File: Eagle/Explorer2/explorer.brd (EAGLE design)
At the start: 101.6 x 66 mm, 10 parts

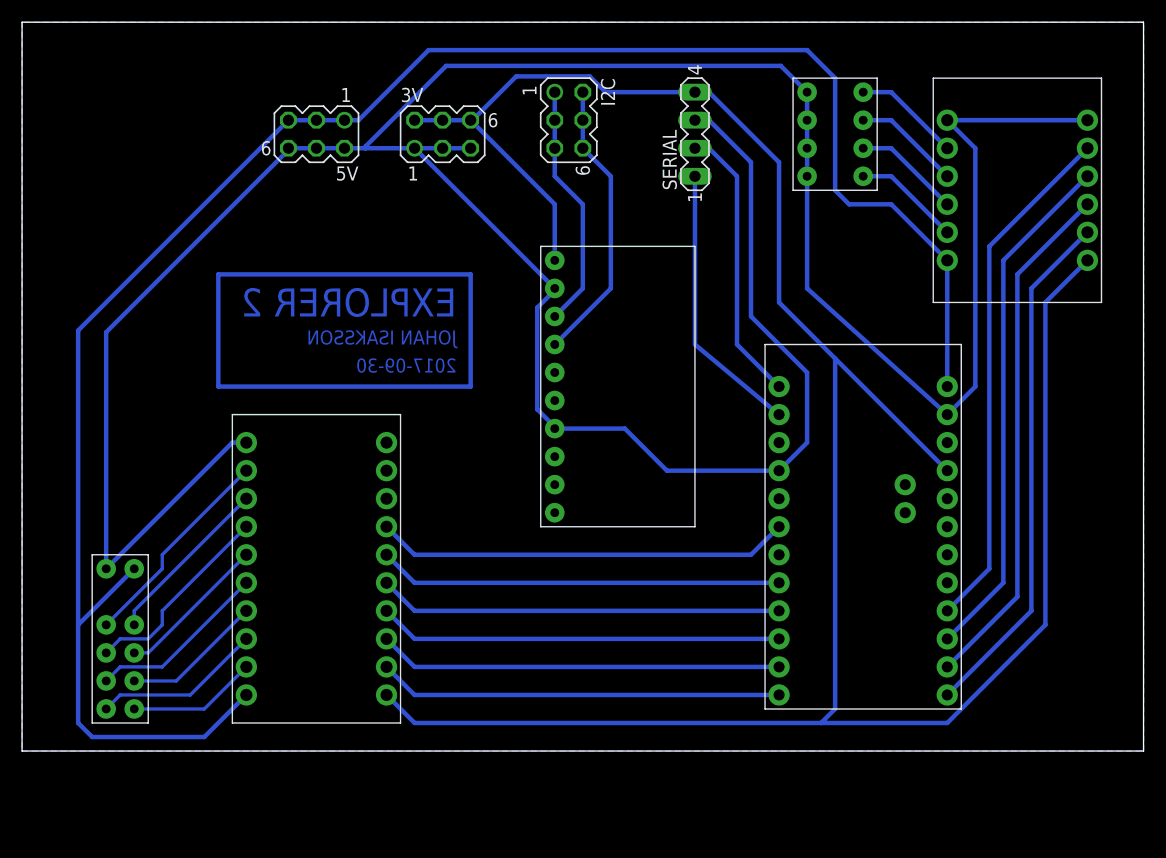
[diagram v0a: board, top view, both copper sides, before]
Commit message: Redesigned Explorer2 board to use two copper layers. Cleaned up and tested Explorer2 code, ready for test.
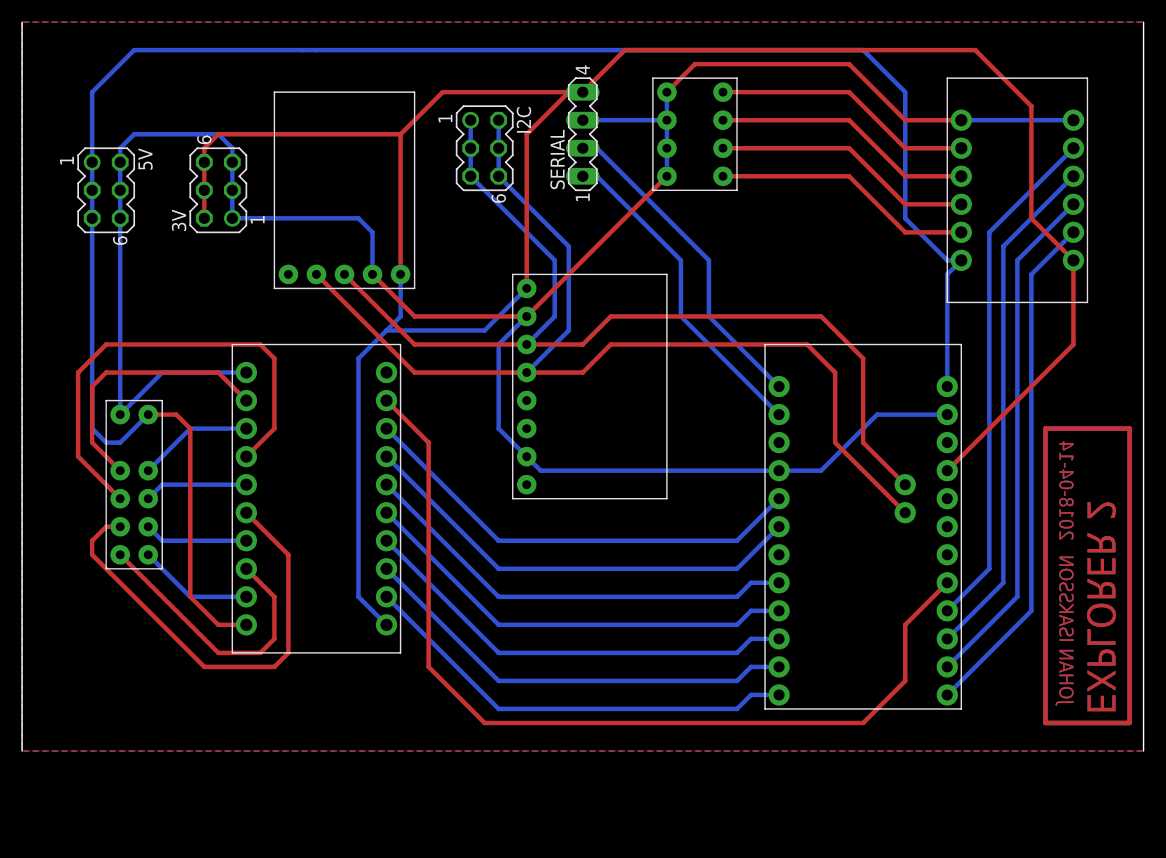
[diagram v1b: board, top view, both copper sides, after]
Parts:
- added U$5: LEVELSHIFT_4CH, quadcopter_comp:LEVELSHIFT_4CH
- U$2: value MPU9250 -> MPU6050; device quadcopter_comp:MPU9250 -> quadcopter_comp:MPU6050
- U$7: value LEVELSHIFT_4CH -> HMC5883L; device quadcopter_comp:LEVELSHIFT_4CH -> quadcopter_comp:HMC5883L
- moved U$7 61.0 mm to (29.2, 50.8), turned to 270 degrees
- moved 3V 20.9 mm to (17.8, 50.8), turned to 90 degrees
- moved 5V 19.7 mm to (7.62, 50.8), turned to 270 degrees
- moved U$6 14.0 mm to (10.2, 24.1)
- moved U$1 12.7 mm to (61.0, 55.9)
- moved SERIAL 10.2 mm to (50.8, 55.9)
- moved I2C 8.03 mm to (41.9, 54.6)
- moved U$4 6.35 mm to (26.7, 22.9)
- moved U$2 2.54 mm to (52.1, 33.0)
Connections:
- new net N$19: U$3.2, U$4.A7
- new net N$25: U$3.A0, U$4.A8
- net 3V: now also U$5.LV, U$7.VCC; no longer U$7.LV
- net 5V: now also U$5.HV; no longer U$7.HV
- net GND: now also U$5.GND, U$5.GND2; no longer U$7.GND2
- net N$1: now also U$5.B4; no longer U$7.B4
- net N$10: now also U$5.A4; no longer U$7.A4
- net N$2: now also U$5.B3; no longer U$7.B3
- net N$26: now also U$7.SCL
- net N$28: now also U$7.SDA
- net N$3: now also U$5.B2; no longer U$7.B2
- net N$4: now also U$5.B1; no longer U$7.B1
- net N$7: now also U$5.A1; no longer U$7.A1
- net N$8: now also U$5.A2; no longer U$7.A2
- net N$9: now also U$5.A3; no longer U$7.A3
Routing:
- net N$25: track 0.00 -> 83.0 mm
- net GND: track 291.0 -> 216.0 mm
- net N$28: track 26.0 -> 95.2 mm
- net N$29: track 0.00 -> 68.6 mm
- net N$27: track 0.00 -> 68.6 mm
- net N$26: track 22.6 -> 89.8 mm
- net N$5: track 66.0 -> 0.00 mm
- net N$19: track 0.00 -> 41.3 mm
- net N$14: track 16.4 -> 41.1 mm
- net N$16: track 18.2 -> 42.3 mm
- net N$4: track 9.72 -> 23.7 mm
- net N$3: track 9.72 -> 23.7 mm
- net N$2: track 9.72 -> 23.7 mm
- net N$1: track 9.72 -> 23.7 mm
- net 3V: track 220.7 -> 207.1 mm
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- added copper zone on layer 1, net GND
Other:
- board text added: "2018-04-14"
- board text removed: "2017-09-30"

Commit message: Replaced all sensor breakout boards with one gy-86 board. Started on pids for altitude hold.
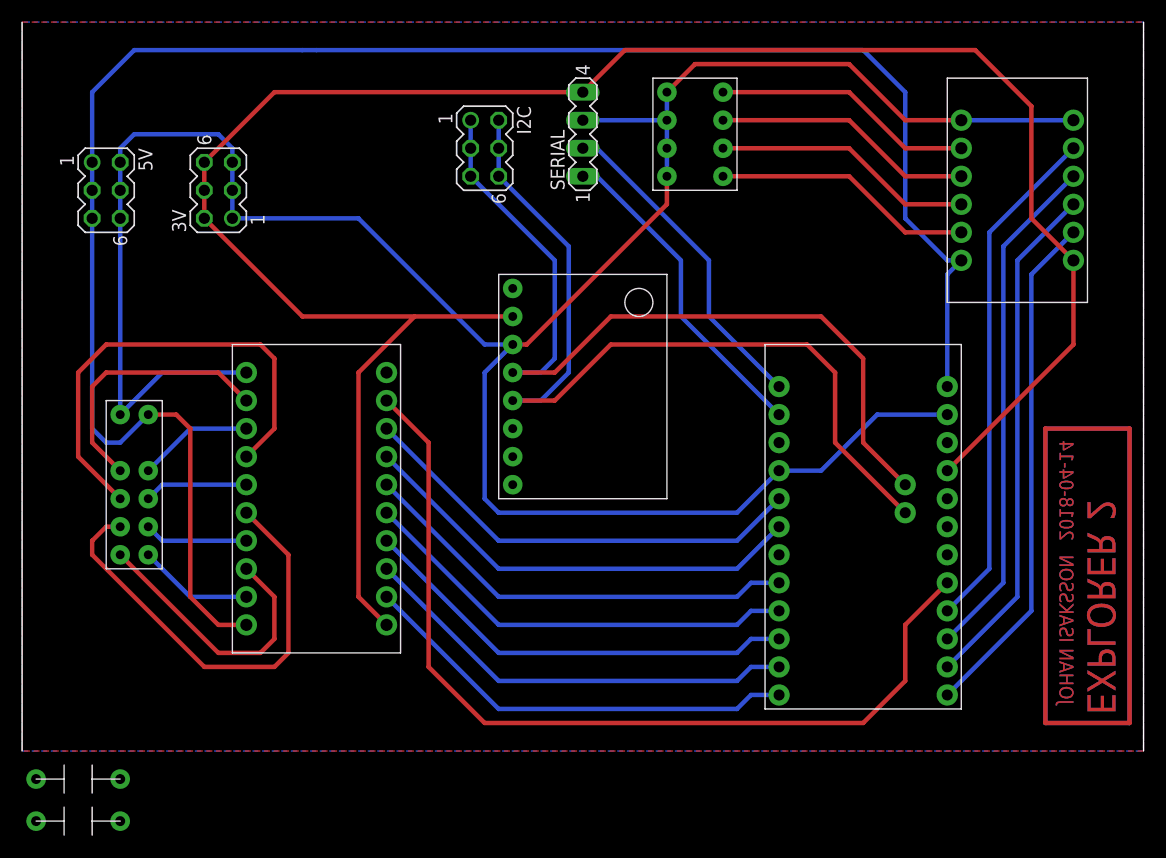
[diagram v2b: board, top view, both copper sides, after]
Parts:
- added U$8: GY-86, quadcopter_comp:GY-86
- U$2: value MPU6050 -> CAP; device quadcopter_comp:MPU6050 -> quadcopter_comp:CAP
- U$7: value HMC5883L -> CAP; device quadcopter_comp:HMC5883L -> quadcopter_comp:CAP
- moved U$7 62.0 mm to (5.08, -6.35), turned to 0 degrees
- moved U$2 58.9 mm to (5.08, -2.54)
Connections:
- net 3V: now also U$8.3V3; no longer U$2.VCC, U$7.VCC
- net 5V: now also U$2.B, U$7.B
- net GND: now also U$2.A, U$7.A, U$8.GND; no longer U$2.AD0, U$2.GND, U$7.GND
- net N$26: now also U$8.SCL; no longer U$2.SCL, U$7.SCL
- net N$28: now also U$8.SDA; no longer U$2.SDA, U$7.SDA
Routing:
- net 3V: track 207.1 -> 188.4 mm
- net N$28: track 95.2 -> 79.3 mm
- net N$26: track 89.8 -> 77.5 mm
- net GND: track 216.0 -> 223.0 mm
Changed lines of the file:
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@@
 <attribute name="MF" value="" x="50.8" y="55.88" size="1.778" layer="27" rot="R90" display="off"/>
 </element>
-<element name="U$2" library="quadcopter_comp" package="MPU6050" value="MPU6050" x="52.07" y="33.02"/>
 <element name="U$5" library="quadcopter_comp" package="LEVELSHIFT_4CH" value="LEVELSHIFT_4CH" x="90.17" y="50.8" rot="R180"/>
-<element name="U$7" library="quadcopter_comp" package="HMC5883L" value="HMC5883L" x="29.21" y="50.8" rot="R270"/>
+<element name="U$8" library="quadcopter_comp" package="GY-86" value="GY-86" x="50.8" y="33.02"/>
+<element name="U$2" library="quadcopter_comp" package="CAP" value="CAP" x="5.08" y="-2.54"/>
+<element name="U$7" library="quadcopter_comp" package="CAP" value="CAP" x="5.08" y="-6.35"/>
 </elements>
 <signals>
@@
 <vertex x="0" y="0"/>
 </polygon>
-<contactref element="U$2" pad="GND"/>
-<contactref element="U$2" pad="AD0"/>
 <contactref element="U$5" pad="GND2"/>
 <contactref element="U$5" pad="GND"/>
@@
 <wire x1="74.93" y1="62.23" x2="60.96" y2="62.23" width="0.4064" layer="1"/>
 <wire x1="60.96" y1="62.23" x2="58.42" y2="59.69" width="0.4064" layer="1"/>
-<wire x1="68.58" y1="25.4" x2="46.99" y2="25.4" width="0.4064" layer="16"/>
-<wire x1="46.99" y1="25.4" x2="45.72" y2="26.67" width="0.4064" layer="16"/>
-<wire x1="45.72" y1="39.37" x2="43.18" y2="36.83" width="0.4064" layer="16"/>
-<wire x1="43.18" y1="36.83" x2="43.18" y2="29.21" width="0.4064" layer="16"/>
-<wire x1="43.18" y1="29.21" x2="45.72" y2="26.67" width="0.4064" layer="16"/>
-<wire x1="45.72" y1="39.37" x2="58.42" y2="52.07" width="0.4064" layer="1"/>
-<contactref element="U$7" pad="GND"/>
 <wire x1="8.89" y1="30.48" x2="8.89" y2="48.26" width="0.4064" layer="16"/>
 <wire x1="8.89" y1="50.8" x2="8.89" y2="48.26" width="0.4064" layer="16"/>
 <wire x1="8.89" y1="53.34" x2="8.89" y2="50.8" width="0.4064" layer="16"/>
-<wire x1="31.75" y1="43.18" x2="31.75" y2="46.99" width="0.4064" layer="16"/>
-<wire x1="31.75" y1="46.99" x2="30.48" y2="48.26" width="0.4064" layer="16"/>
 <wire x1="30.48" y1="48.26" x2="19.05" y2="48.26" width="0.4064" layer="16"/>
 <wire x1="19.05" y1="50.8" x2="19.05" y2="48.26" width="0.4064" layer="16"/>
@@
 <wire x1="17.78" y1="55.88" x2="19.05" y2="54.61" width="0.4064" layer="16"/>
 <wire x1="19.05" y1="54.61" x2="19.05" y2="53.34" width="0.4064" layer="16"/>
-<wire x1="31.75" y1="43.18" x2="35.56" y2="39.37" width="0.4064" layer="1"/>
-<wire x1="35.56" y1="39.37" x2="45.72" y2="39.37" width="0.4064" layer="1"/>
+<contactref element="U$8" pad="GND"/>
+<wire x1="30.48" y1="48.26" x2="41.91" y2="36.83" width="0.4064" layer="16"/>
+<wire x1="41.91" y1="36.83" x2="44.45" y2="36.83" width="0.4064" layer="16"/>
+<wire x1="44.45" y1="36.83" x2="45.72" y2="36.83" width="0.4064" layer="1"/>
+<wire x1="45.72" y1="36.83" x2="58.42" y2="49.53" width="0.4064" layer="1"/>
+<wire x1="58.42" y1="49.53" x2="58.42" y2="52.07" width="0.4064" layer="1"/>
+<wire x1="44.45" y1="36.83" x2="41.91" y2="34.29" width="0.4064" layer="16"/>
+<wire x1="41.91" y1="34.29" x2="41.91" y2="22.86" width="0.4064" layer="16"/>
+<wire x1="41.91" y1="22.86" x2="43.18" y2="21.59" width="0.4064" layer="16"/>
+<wire x1="43.18" y1="21.59" x2="64.77" y2="21.59" width="0.4064" layer="16"/>
+<wire x1="64.77" y1="21.59" x2="68.58" y2="25.4" width="0.4064" layer="16"/>
+<contactref element="U$2" pad="A"/>
+<contactref element="U$7" pad="A"/>
+<wire x1="1.27" y1="-2.54" x2="8.89" y2="30.48" width="0" layer="19" extent="1-1"/>
+<wire x1="1.27" y1="-6.35" x2="1.27" y2="-2.54" width="0" layer="19" extent="1-1"/>
 </signal>
 <signal name="N$20">
@@
 <wire x1="6.35" y1="59.69" x2="10.16" y2="63.5" width="0.4064" layer="16"/>
 <wire x1="10.16" y1="63.5" x2="25.4" y2="63.5" width="0.4064" layer="16"/>
+<contactref element="U$2" pad="B"/>
+<contactref element="U$7" pad="B"/>
+<wire x1="8.89" y1="-2.54" x2="17.78" y2="11.43" width="0" layer="19" extent="1-1"/>
+<wire x1="8.89" y1="-6.35" x2="8.89" y2="-2.54" width="0" layer="19" extent="1-1"/>
 </signal>
 <signal name="3V">
@@
 <contactref element="3V" pad="4"/>
 <contactref element="SERIAL" pad="4"/>
-<wire x1="33.02" y1="11.43" x2="30.48" y2="13.97" width="0.4064" layer="16"/>
-<wire x1="30.48" y1="13.97" x2="30.48" y2="35.56" width="0.4064" layer="16"/>
-<wire x1="30.48" y1="35.56" x2="33.02" y2="38.1" width="0.4064" layer="16"/>
-<wire x1="33.02" y1="38.1" x2="41.91" y2="38.1" width="0.4064" layer="16"/>
-<wire x1="34.29" y1="55.88" x2="38.1" y2="59.69" width="0.4064" layer="1"/>
-<wire x1="38.1" y1="59.69" x2="49.53" y2="59.69" width="0.4064" layer="1"/>
-<wire x1="49.53" y1="59.69" x2="50.8" y2="59.69" width="0.4064" layer="1"/>
 <wire x1="54.61" y1="63.5" x2="50.8" y2="59.69" width="0.4064" layer="1"/>
-<contactref element="U$2" pad="VCC"/>
 <contactref element="U$5" pad="LV"/>
 <wire x1="54.61" y1="63.5" x2="86.36" y2="63.5" width="0.4064" layer="1"/>
@@
 <wire x1="95.25" y1="44.45" x2="95.25" y2="36.83" width="0.4064" layer="1"/>
 <wire x1="95.25" y1="36.83" x2="83.82" y2="25.4" width="0.4064" layer="1"/>
-<wire x1="41.91" y1="38.1" x2="45.72" y2="41.91" width="0.4064" layer="16"/>
-<wire x1="45.72" y1="41.91" x2="45.72" y2="55.88" width="0.4064" layer="1"/>
-<wire x1="45.72" y1="55.88" x2="49.53" y2="59.69" width="0.4064" layer="1"/>
-<contactref element="U$7" pad="VCC"/>
-<wire x1="34.29" y1="43.18" x2="34.29" y2="39.37" width="0.4064" layer="16"/>
-<wire x1="34.29" y1="39.37" x2="33.02" y2="38.1" width="0.4064" layer="16"/>
 <wire x1="16.51" y1="53.34" x2="16.51" y2="50.8" width="0.4064" layer="1"/>
-<wire x1="34.29" y1="43.18" x2="34.29" y2="55.88" width="0.4064" layer="1"/>
-<wire x1="16.51" y1="53.34" x2="16.51" y2="54.61" width="0.4064" layer="1"/>
-<wire x1="16.51" y1="54.61" x2="17.78" y2="55.88" width="0.4064" layer="1"/>
-<wire x1="17.78" y1="55.88" x2="34.29" y2="55.88" width="0.4064" layer="1"/>
 <wire x1="16.51" y1="50.8" x2="16.51" y2="48.26" width="0.4064" layer="1"/>
+<contactref element="U$8" pad="3V3"/>
+<wire x1="22.86" y1="59.69" x2="16.51" y2="53.34" width="0.4064" layer="1"/>
+<wire x1="50.8" y1="59.69" x2="22.86" y2="59.69" width="0.4064" layer="1"/>
+<wire x1="44.45" y1="39.37" x2="35.56" y2="39.37" width="0.4064" layer="1"/>
+<wire x1="35.56" y1="39.37" x2="25.4" y2="39.37" width="0.4064" layer="1"/>
+<wire x1="25.4" y1="39.37" x2="16.51" y2="48.26" width="0.4064" layer="1"/>
+<wire x1="33.02" y1="11.43" x2="30.48" y2="13.97" width="0.4064" layer="1"/>
+<wire x1="30.48" y1="13.97" x2="30.48" y2="34.29" width="0.4064" layer="1"/>
+<wire x1="30.48" y1="34.29" x2="35.56" y2="39.37" width="0.4064" layer="1"/>
 </signal>
 <signal name="N$26">
@@
 <wire x1="76.2" y1="27.94" x2="76.2" y2="35.56" width="0.4064" layer="1"/>
 <wire x1="76.2" y1="35.56" x2="72.39" y2="39.37" width="0.4064" layer="1"/>
-<contactref element="U$2" pad="SCL"/>
 <wire x1="72.39" y1="39.37" x2="53.34" y2="39.37" width="0.4064" layer="1"/>
-<wire x1="53.34" y1="39.37" x2="50.8" y2="36.83" width="0.4064" layer="1"/>
-<wire x1="50.8" y1="36.83" x2="45.72" y2="36.83" width="0.4064" layer="1"/>
 <wire x1="40.64" y1="52.07" x2="48.26" y2="44.45" width="0.4064" layer="16"/>
-<wire x1="48.26" y1="44.45" x2="48.26" y2="39.37" width="0.4064" layer="16"/>
-<wire x1="48.26" y1="39.37" x2="45.72" y2="36.83" width="0.4064" layer="16"/>
-<contactref element="U$7" pad="SCL"/>
-<wire x1="45.72" y1="36.83" x2="35.56" y2="36.83" width="0.4064" layer="1"/>
-<wire x1="35.56" y1="36.83" x2="29.21" y2="43.18" width="0.4064" layer="1"/>
+<wire x1="48.26" y1="44.45" x2="48.26" y2="35.56" width="0.4064" layer="16"/>
+<contactref element="U$8" pad="SCL"/>
+<wire x1="53.34" y1="39.37" x2="48.26" y2="34.29" width="0.4064" layer="1"/>
+<wire x1="48.26" y1="34.29" x2="44.45" y2="34.29" width="0.4064" layer="1"/>
+<wire x1="48.26" y1="35.56" x2="46.99" y2="34.29" width="0.4064" layer="16"/>
+<wire x1="46.99" y1="34.29" x2="44.45" y2="34.29" width="0.4064" layer="16"/>
 </signal>
 <signal name="N$28">
@@
 <wire x1="73.66" y1="27.94" x2="73.66" y2="34.29" width="0.4064" layer="1"/>
 <wire x1="73.66" y1="34.29" x2="71.12" y2="36.83" width="0.4064" layer="1"/>
-<contactref element="U$2" pad="SDA"/>
 <wire x1="71.12" y1="36.83" x2="53.34" y2="36.83" width="0.4064" layer="1"/>
-<wire x1="53.34" y1="36.83" x2="50.8" y2="34.29" width="0.4064" layer="1"/>
-<wire x1="50.8" y1="34.29" x2="45.72" y2="34.29" width="0.4064" layer="1"/>
 <wire x1="43.18" y1="52.07" x2="49.53" y2="45.72" width="0.4064" layer="16"/>
-<wire x1="49.53" y1="45.72" x2="49.53" y2="38.1" width="0.4064" layer="16"/>
-<wire x1="49.53" y1="38.1" x2="45.72" y2="34.29" width="0.4064" layer="16"/>
-<contactref element="U$7" pad="SDA"/>
-<wire x1="45.72" y1="34.29" x2="35.56" y2="34.29" width="0.4064" layer="1"/>
-<wire x1="35.56" y1="34.29" x2="26.67" y2="43.18" width="0.4064" layer="1"/>
+<wire x1="49.53" y1="45.72" x2="49.53" y2="34.29" width="0.4064" layer="16"/>
+<contactref element="U$8" pad="SDA"/>
+<wire x1="53.34" y1="36.83" x2="48.26" y2="31.75" width="0.4064" layer="1"/>
+<wire x1="48.26" y1="31.75" x2="44.45" y2="31.75" width="0.4064" layer="1"/>
+<wire x1="49.53" y1="34.29" x2="46.99" y2="31.75" width="0.4064" layer="16"/>
+<wire x1="46.99" y1="31.75" x2="44.45" y2="31.75" width="0.4064" layer="16"/>
 </signal>
 <signal name="N$33">
